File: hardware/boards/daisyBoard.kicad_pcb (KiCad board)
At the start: 4 copper layers, 100 x 100 mm, 112 parts, among them IC1 TL072, IC2 TL072, IC3 TL072, IC4 TL072, J1 LEFT Pin ROW, J13 LEFT Pin ROW Daisy, J14 RIGHT Pin ROW DAISY, J15 Daisy Pin Breakout LEFT, J16 Daisy PIN Breakout RIGHT, J2 RIGHT Pin Row, J3 ESP32 Pin Breakout RIGHT, J4 ESP32 Pin Breakout LEFT, U1 MCP6002-xSN, U2 MCP6002-xSN, U3 MCP6002-xSN

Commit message: alignment changes
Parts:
- FB1: value 60R @ 100MHz -> 600 Ω @ 100 MHz
- moved FB1 3.15 mm to (101.9, 70.6)
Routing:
- net +5V: track 93.1 -> 96.6 mm
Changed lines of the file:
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@@
 			)
 		)
-		(attr board_only exclude_from_pos_files exclude_from_bom)
+		(attr board_only exclude_from_bom)
 		(duplicate_pad_numbers_are_jumpers no)
 		(fp_poly
@@
 			)
 		)
-		(attr exclude_from_bom)
 		(duplicate_pad_numbers_are_jumpers no)
 		(fp_line
@@
 			)
 		)
+		(attr exclude_from_pos_files)
 		(duplicate_pad_numbers_are_jumpers no)
 		(fp_circle
@@
 	(footprint "Inductor_SMD:L_0805_2012Metric"
 		(layer "F.Cu")
-		(at 104.5925 68.9 180)
+		(at 101.9375 70.6 180)
 		(descr "Inductor SMD 0805 (2012 Metric), square (rectangular) end terminal, IPC-7351 nominal, (Body size source: IPC-SM-782 page 80, https://www.pcb-3d.com/wordpress/wp-content/uploads/ipc-sm-782a_amendment_1_and_2.pdf)")
 		(tags "inductor")
 		(property "Reference" "FB1"
-			(at 3.45 0.12 0)
+			(at -4 0.2 0)
 			(layer "F.SilkS")
 			(effects
@@
 			)
 		)
-		(property "Value" "60R @ 100MHz"
+		(property "Value" "600 Ω @ 100 MHz"
 			(at 0.82 -1.73 0)
 			(layer "F.Fab")
@@
 			)
 		)
-		(property "LCSC" "C405006"
+		(property "LCSC" "C51018430"
 			(at 0 0 0)
 			(layer "F.SilkS")
@@
 			)
 		)
-		(attr exclude_from_bom)
 		(duplicate_pad_numbers_are_jumpers no)
 		(fp_line
@@
 	)
 	(via
-		(at 103.7025 68.87)
+		(at 100.875 70.6)
 		(size 0.6858)
 		(drill 0.3302)
@@
 	)
 	(segment
+		(start 103.7025 72.965)
+		(end 103.7025 73.2175)
+		(width 0.508)
+		(layer "In2.Cu")
+		(net "VCC_ESP32")
+	)
+	(segment
 		(start 98.58 84.564868)
 		(end 100.090559 83.054309)
@@
 	)
 	(segment
-		(start 103.7025 68.87)
-		(end 103.7025 73.2175)
+		(start 103.7025 73.2175)
+		(end 103.55 73.37)
 		(width 0.508)
 		(layer "In2.Cu")
@@
 	)
 	(segment
-		(start 103.7025 73.2175)
-		(end 103.55 73.37)
-		(width 0.508)
-		(layer "In2.Cu")
-		(net "VCC_ESP32")
-	)
-	(segment
 		(start 64.23 89.07)
 		(end 64.23 91.23)
@@
 	)
 	(segment
+		(start 100.875 70.6)
+		(end 101.3375 70.6)
+		(width 0.508)
+		(layer "In2.Cu")
+		(net "VCC_ESP32")
+	)
+	(segment
 		(start 65.5 92.5)
 		(end 95 92.5)
@@
 	)
 	(segment
+		(start 101.3375 70.6)
+		(end 103.7025 72.965)
+		(width 0.508)
+		(layer "In2.Cu")
+		(net "VCC_ESP32")
+	)
+	(segment
 		(start 103.55 79.594868)
 		(end 103.322434 79.822434)
@@
 	)
 	(via
-		(at 105.8275 68.87)
+		(at 103 70.6)
 		(size 0.6858)
 		(drill 0.3302)
@@
 	)
 	(segment
-		(start 105.8275 68.87)
-		(end 105.85 68.87)
+		(start 103 70.5)
+		(end 103.2 70.5)
 		(width 0.762)
 		(layer "In2.Cu")
@@
 	)
 	(segment
-		(start 114.72 60)
-		(end 128 60)
-		(width 0.762)
-		(layer "In2.Cu")
-		(net "+5V")
-	)
-	(segment
 		(start 127.84 61.8)
 		(end 117.8525 61.8)
@@
 	)
 	(segment
-		(start 128 60)
-		(end 131.34 56.66)
-		(width 0.762)
-		(layer "In2.Cu")
-		(net "+5V")
-	)
-	(segment
 		(start 112.0109 80.1859)
 		(end 112.0109 65.1891)
@@
 	)
 	(segment
-		(start 105.85 68.87)
-		(end 114.72 60)
+		(start 112.0109 65.1891)
+		(end 115.4 61.8)
 		(width 0.762)
 		(layer "In2.Cu")
@@
 	)
 	(segment
-		(start 112.0109 65.1891)
-		(end 115.4 61.8)
+		(start 128 60)
+		(end 131.34 56.66)
 		(width 0.762)
 		(layer "In2.Cu")
@@
 		(width 0.762)
 		(layer "In2.Cu")
+		(net "+5V")
+	)
+	(segment
+		(start 103.2 70.5)
+		(end 113.7 60)
+		(width 0.762)
+		(layer "In2.Cu")
+		(net "+5V")
+	)
+	(segment
+		(start 113.7 60)
+		(end 128 60)
+		(width 0.762)
+		(layer "In2.Cu")

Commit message: added some changes and checks adnd did a review
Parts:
- added C18: 100nF, Capacitor_SMD:C_1206_3216Metric, F.Cu at (81.0, 99.1)
- added C26: 100nF, Capacitor_SMD:C_1206_3216Metric, F.Cu at (63.2, 109.6)
- added C27: 100nF, Capacitor_SMD:C_1206_3216Metric, F.Cu at (80.3, 122.8)
- added C28: 100nF, Capacitor_SMD:C_1206_3216Metric, F.Cu at (63.8, 134.1)
- added C29: 100nF, Capacitor_SMD:C_1206_3216Metric, F.Cu at (91.8, 129.1)
- added C30: 100nF, Capacitor_SMD:C_1206_3216Metric, F.Cu at (98.0, 133.1)
- added C31: 100nF, Capacitor_SMD:C_1206_3216Metric, F.Cu at (118.6, 83.2)
- C32: renamed from 100nF1; value C26 -> 100nF
- moved TP5 4.62 mm to (121.0, 79.0)
- turned FB1 to 0 degrees
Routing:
- net VCC_Daisy: track 112.7 -> 134.7 mm
- net +5V: track 96.6 -> 102.0 mm
- net ESP-3.3V: track 12.2 -> 16.3 mm
- net VREF: track 120.9 -> 118.7 mm
- net VCC_ESP32: track 67.9 -> 66.7 mm
- net Net-(U2B-+): track 13.5 -> 14.1 mm
- net GND: vias 42 -> 51

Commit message: updated TL072 to the H model in order to account ofr the 5V in that is currently lower than the 7V TL072 operating range
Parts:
- IC1, IC2, IC3, IC4: value TL072 -> TL072HIDR
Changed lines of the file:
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@@
 			)
 		)
-		(property "Value" "TL072"
+		(property "Value" "TL072HIDR"
 			(at 0 3.4 90)
 			(layer "F.Fab")
@@
 			)
 		)
-		(property "Datasheet" "http://www.ti.com/lit/ds/symlink/tl071.pdf"
+		(property "Datasheet" "https://www.ti.com/cn/lit/gpn/tl074a"
 			(at 0 0 90)
 			(layer "F.Fab")
@@
 			)
 		)
-		(property "LCSC" "C1346149"
+		(property "LCSC" "C4370389"
 			(at 0 0 0)
 			(layer "F.SilkS")
@@
 			)
 		)
-		(property "Value" "TL072"
+		(property "Value" "TL072HIDR"
 			(at 4.5 -0.075 180)
 			(layer "F.Fab")
@@
 			)
 		)
-		(property "Datasheet" "http://www.ti.com/lit/ds/symlink/tl071.pdf"
+		(property "Datasheet" "https://www.ti.com/cn/lit/gpn/tl074a"
 			(at 0 0 90)
 			(layer "F.Fab")
@@
 			)
 		)
-		(property "LCSC" "C1346149"
+		(property "LCSC" "C4370389"
 			(at 0 0 0)
 			(layer "F.SilkS")
@@
 			)
 		)
-		(property "Value" "TL072"
+		(property "Value" "TL072HIDR"
 			(at 0 3.4 0)
 			(layer "F.Fab")
@@
 			)
 		)
-		(property "Datasheet" "http://www.ti.com/lit/ds/symlink/tl071.pdf"
+		(property "Datasheet" "https://www.ti.com/cn/lit/gpn/tl074a"
 			(at 0 0 0)
 			(layer "F.Fab")
@@
 			)
 		)
-		(property "LCSC" "C1346149"
+		(property "LCSC" "C4370389"
 			(at 0 0 0)
 			(layer "F.SilkS")
@@
 			)
 		)
-		(property "Value" "TL072"
+		(property "Value" "TL072HIDR"
 			(at 0 3.4 0)
 			(layer "F.Fab")
@@
 			)
 		)
-		(property "Datasheet" "http://www.ti.com/lit/ds/symlink/tl071.pdf"
+		(property "Datasheet" "https://www.ti.com/cn/lit/gpn/tl074a"
 			(at 0 0 0)
 			(layer "F.Fab")
@@
 			)
 		)
-		(property "LCSC" "C1346149"
+		(property "LCSC" "C4370389"
 			(at 0 0 0)
 			(layer "F.SilkS")

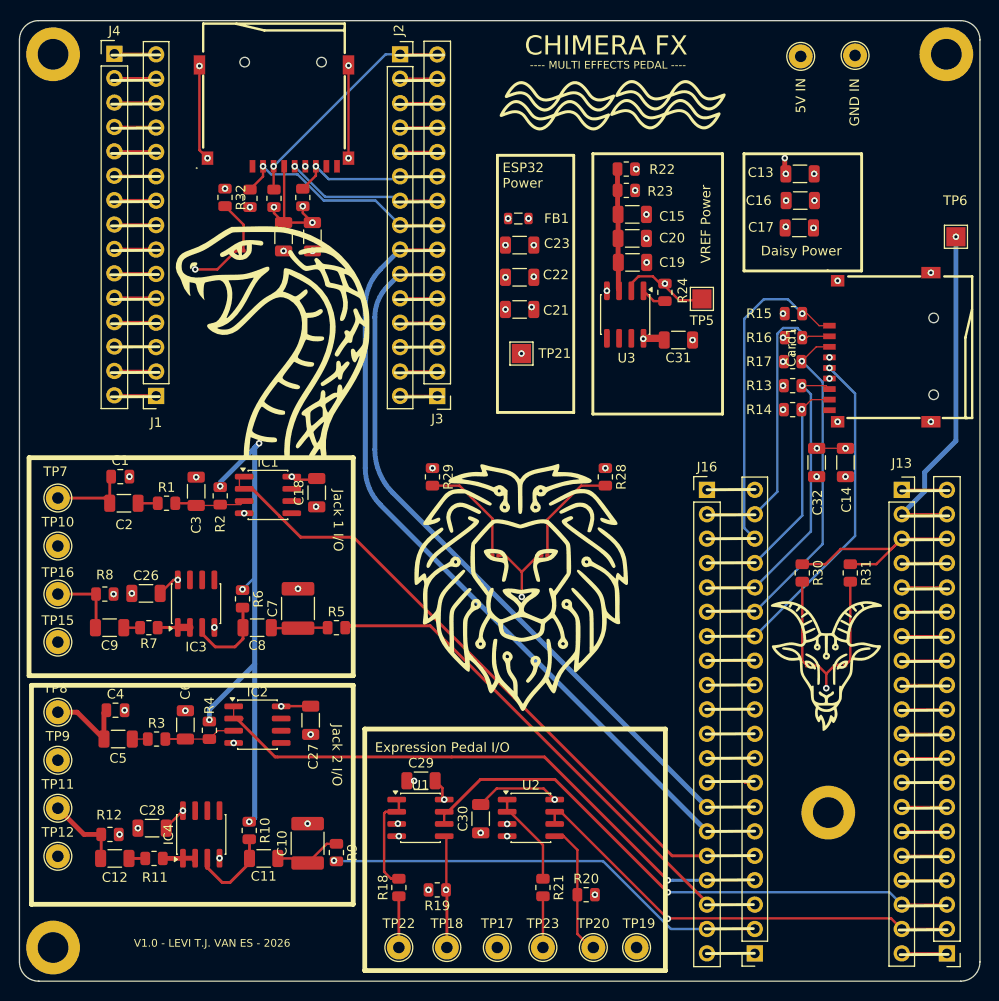
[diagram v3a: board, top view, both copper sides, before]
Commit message: moved some pads again
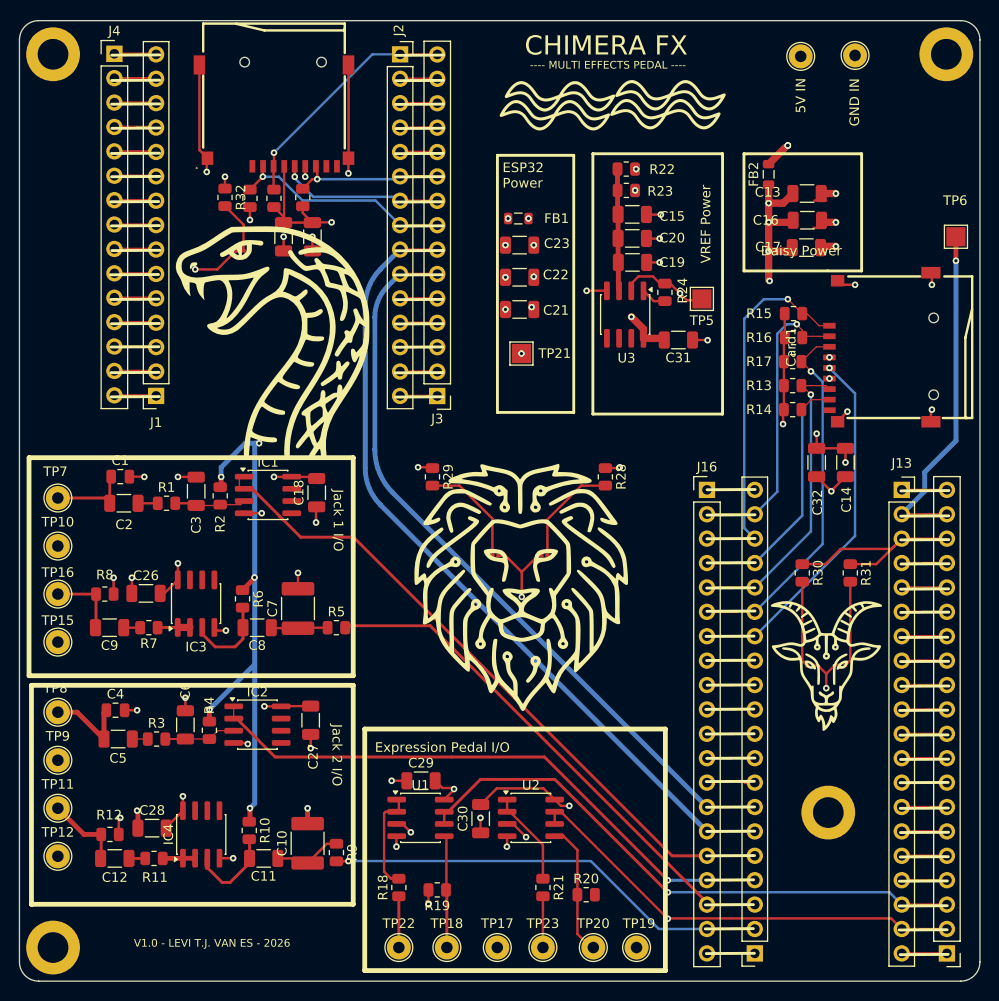
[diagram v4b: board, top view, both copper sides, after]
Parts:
- removed NT1: NetTie_2, NetTie:NetTie-2_SMD_Pad0.5mm
- added FB2: 600 Ω @ 100 MHz, Inductor_SMD:L_0805_2012Metric, F.Cu at (128.0, 66.0)
- moved C13 2.18 mm to (132.0, 68.0)
- moved C16 2.18 mm to (132.0, 70.8)
- moved C17 2.18 mm to (131.9, 73.6)
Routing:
- net GND: track 56.8 -> 122.1 mm, vias 51 -> 47
- net VCC_Daisy: track 134.7 -> 149.9 mm, vias 12 -> 13
- net ESP-3.3V: track 16.3 -> 21.0 mm, vias 5 -> 3
- net +3.3VD: track 83.3 -> 80.8 mm, vias 8 -> 4
- net /AUDIO_OUT_2: track 47.6 -> 46.7 mm
- net +5V: track 102.0 -> 103.0 mm, vias 4 -> 5
- net /SD_MOSI: track 24.3 -> 25.3 mm
- net /SD_SCK: track 16.3 -> 17.1 mm
- net +3.3VA: track 69.3 -> 70.0 mm
- net /SD_DAT_3_DAISY: track 31.3 -> 31.8 mm
- net Net-(U1B-+): vias 1 -> 0
- net /SD_DAT_1_DAISY: vias 1 -> 0

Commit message: did drc checks fix and connected flaoting pins on op amps
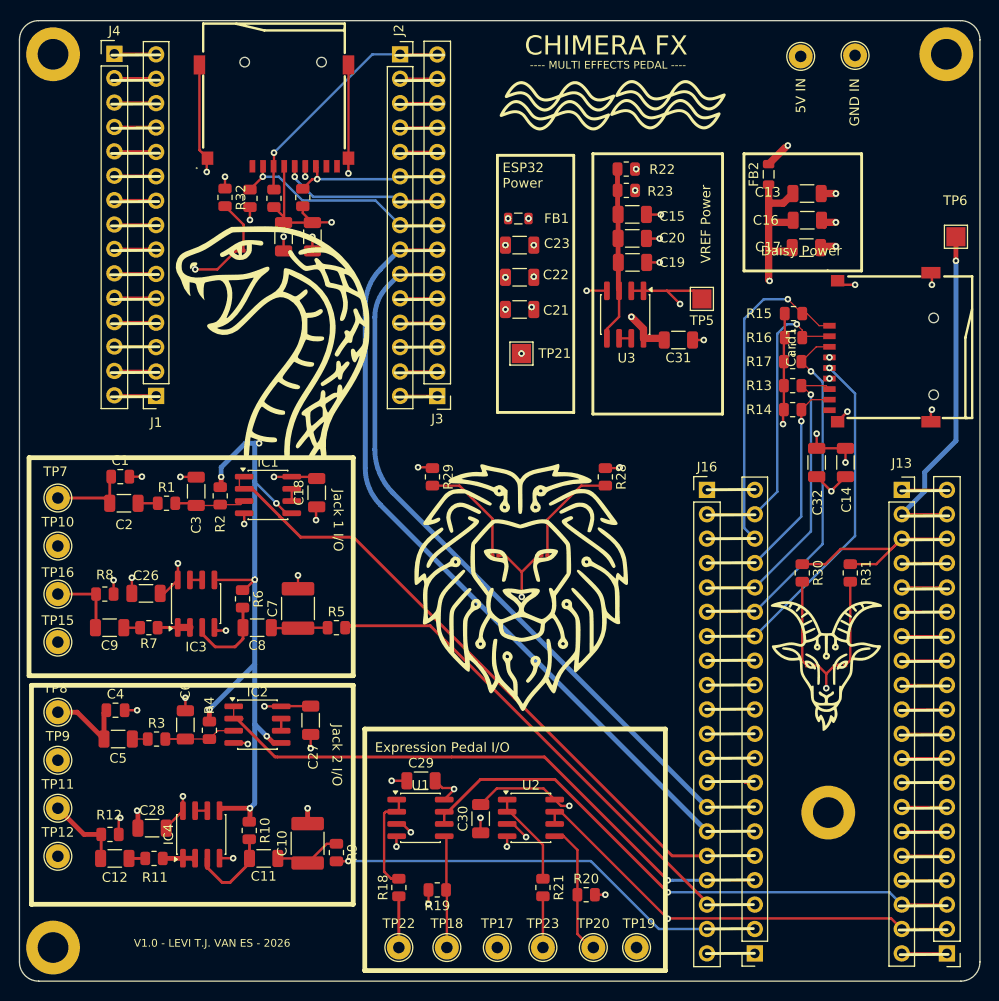
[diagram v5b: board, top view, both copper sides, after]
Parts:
- removed R24: 100R, Resistor_SMD:R_0805_2012Metric
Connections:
- IC1 pad 5: unconnected-(IC1B-+-Pad5) -> VREF
- IC1 pad 6: unconnected-(IC1B---Pad6) -> Net-(IC1B--)
- IC1 pad 7: unconnected-(IC1-Pad7) -> Net-(IC1B--)
- IC2 pad 5: unconnected-(IC2B-+-Pad5) -> VREF
- IC2 pad 6: unconnected-(IC2B---Pad6) -> Net-(IC2B--)
- IC2 pad 7: unconnected-(IC2-Pad7) -> Net-(IC2B--)
- IC3 pad 5: unconnected-(IC3B-+-Pad5) -> VREF
- IC3 pad 6: unconnected-(IC3B---Pad6) -> Net-(IC3B--)
- IC3 pad 7: unconnected-(IC3-Pad7) -> Net-(IC3B--)
- IC4 pad 5: unconnected-(IC4B-+-Pad5) -> VREF
- IC4 pad 6: unconnected-(IC4B---Pad6) -> Net-(IC4B--)
- IC4 pad 7: unconnected-(IC4-Pad7) -> Net-(IC4B--)
- U3 pad 1: Net-(R24-Pad1) -> VREF
- U3 pad 5: unconnected-(U3B-+-Pad5) -> Net-(U3A-+)
- U3 pad 6: unconnected-(U3B---Pad6) -> Net-(U3B--)
- U3 pad 7: unconnected-(U3-Pad7) -> Net-(U3B--)
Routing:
- net VREF: track 118.7 -> 134.2 mm, vias 6 -> 8
- net Net-(U3A-+): track 14.0 -> 19.5 mm
- net GND: track 122.1 -> 118.4 mm, vias 47 -> 48
- net Net-(R24-Pad1): track 2.18 -> 0.00 mm
- net Net-(IC2B--): track 0.00 -> 1.27 mm
- net Net-(U3B--): track 0.00 -> 1.27 mm
- net Net-(IC4B--): track 0.00 -> 1.27 mm
- net Net-(IC3B--): track 0.00 -> 1.27 mm
- net Net-(IC1B--): track 0.00 -> 1.27 mm
- net /SD_DAT_1_DAISY: vias 0 -> 1
- net VCC_Daisy: vias 13 -> 10
- net +5V: vias 5 -> 4
